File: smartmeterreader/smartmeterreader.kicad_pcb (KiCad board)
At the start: 2 copper layers, 54 x 44 mm, 50 parts, among them J1 USB_B_Micro_RA, J2 RJ12, Q1 2N7002NXBK, Q2 2N7002NXBK, Q3 PMV75UP, Q4 2N7002NXBK, Q5 PMV75UP, Q6 2N7002NXBK, SW1 SPST_NO, SW2 SPST_NO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

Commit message: Sync PCB with schematics
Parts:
- added D1: PMEG2010ER, Diode_SMD:D_SOD-123, F.Cu at (125.5, 90.2)
- added D7: Green, LED_SMD:LED_0603_1608Metric, F.Cu at (140.8, 93.2)
- added D8: Green, LED_SMD:LED_0603_1608Metric, F.Cu at (147.3, 103.8)
- added F1: 1A, Fuse:Fuse_1206_3216Metric, F.Cu at (130.2, 87.5)
- added F2: 1A, Fuse:Fuse_1206_3216Metric, F.Cu at (133.5, 109.2)
- added J3: 1x05_Pin_2.54mm, Connector_PinHeader_2.54mm:PinHeader_1x05_P2.54mm_Vertical, F.Cu at (146.8, 86.8)
- added R20: 1K, Resistor_SMD:R_0603_1608Metric, F.Cu at (140.7, 95.0)
- added R21: 1K, Resistor_SMD:R_0603_1608Metric, F.Cu at (147.3, 102.2)
- added REF**: MountingHole_2.5mm, MountingHole:MountingHole_2.5mm, F.Cu at (141.0, 77.2)
- added REF**: MountingHole_2.5mm, MountingHole:MountingHole_2.5mm, F.Cu at (166.0, 115.8)
- JP1, JP2: moved to B.Cu
- SW1, SW2: footprint Button_Switch_SMD:SW_Push_1P1T_NO_CK_KMR2 -> MECH_Switch_SMD:SW_Push_1P1T_NO_CK_KMR2
- moved R16 50.1 mm to (123.8, 75.8), turned to 0 degrees
- moved JP1 48.9 mm to (146.6, 112.5), turned to 90 degrees
- moved JP2 44.2 mm to (146.6, 110.0), turned to 90 degrees
- moved C9 43.1 mm to (123.8, 77.8), turned to 0 degrees
- moved R11 33.6 mm to (158.6, 78.0), turned to 0 degrees
- moved Q5 31.6 mm to (153.4, 80.7), turned to 0 degrees
- moved R18 30.4 mm to (150.8, 80.7)
- moved C1 30.3 mm to (153.7, 90.2)
- moved R10 29.2 mm to (132.2, 79.2), turned to 180 degrees
- moved Q2 28.2 mm to (142.7, 86.8), turned to 0 degrees
- moved R17 28.1 mm to (140.8, 101.4)
- moved C10 27.1 mm to (163.6, 78.0), turned to 0 degrees
- moved D6 26.9 mm to (129.0, 79.2)
- moved R14 26.8 mm to (133.2, 113.0)
- moved Q3 26.0 mm to (138.2, 105.3), turned to 180 degrees
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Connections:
- D3 pad 3: (no net) -> unconnected-(D3-Pad3)
- D3 pad 4: (no net) -> unconnected-(D3-Pad4)
- D4 pad 3: (no net) -> /DATA_LINE
- D4 pad 4: /DATA_LINE -> unconnected-(D4-Pad4)
- D4 pad 6: (no net) -> unconnected-(D4-Pad6)
- J1 pad 1: /5V_USB -> Net-(J1-Pad1)
- J1 pad 4: (no net) -> unconnected-(J1-Pad4)
- J2 pad 1: /5V_meter -> Net-(J2-Pad1)
- J2 pad 4: (no net) -> unconnected-(J2-Pad4)
- U1 pad 10: (no net) -> unconnected-(U1-Pad10)
- U1 pad 11: (no net) -> unconnected-(U1-Pad11)
- U1 pad 12: (no net) -> unconnected-(U1-Pad12)
- U1 pad 13: (no net) -> Net-(U1-Pad13)
- U1 pad 14: (no net) -> unconnected-(U1-Pad14)
- U1 pad 17: (no net) -> unconnected-(U1-Pad17)
- U1 pad 2: (no net) -> unconnected-(U1-Pad2)
- U1 pad 5: (no net) -> unconnected-(U1-Pad5)
- U1 pad 7: (no net) -> unconnected-(U1-Pad7)
- U1 pad 9: (no net) -> unconnected-(U1-Pad9)
- U2 pad 1: (no net) -> unconnected-(U2-Pad1)
- U2 pad 10: (no net) -> unconnected-(U2-Pad10)
- U2 pad 11: (no net) -> unconnected-(U2-Pad11)
- U2 pad 12: (no net) -> unconnected-(U2-Pad12)
- U2 pad 15: (no net) -> unconnected-(U2-Pad15)
- U2 pad 16: (no net) -> unconnected-(U2-Pad16)
- U2 pad 17: (no net) -> unconnected-(U2-Pad17)
- U2 pad 18: (no net) -> /USB-UART-transceiver/UART_CTS
- U2 pad 22: (no net) -> /USB-UART-transceiver/UART_DSR
- U2 pad 24: (no net) -> unconnected-(U2-Pad24)
- U4 pad 3: (no net) -> unconnected-(U4-Pad3)
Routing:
- net +3V3: track 0.00 -> 76.5 mm, vias 0 -> 8
- net /Data_line_TTL: track 0.00 -> 54.8 mm, vias 0 -> 1
- net GND: track 0.00 -> 53.9 mm, vias 0 -> 27
- net /GPIO0: track 0.00 -> 53.4 mm
- net /UART_RX: track 0.00 -> 53.0 mm, vias 0 -> 1
- net /5V_USB: track 0.00 -> 43.9 mm, vias 0 -> 2
- net /UART_RTS: track 0.00 -> 41.8 mm, vias 0 -> 1
- net /5V_meter: track 0.00 -> 41.0 mm
- net /nRST: track 0.00 -> 40.0 mm, vias 0 -> 2
- net /DHT22_DATA: track 0.00 -> 37.2 mm
- net /UART_TX: track 0.00 -> 27.8 mm, vias 0 -> 2
- net /DATA_LINE: track 0.00 -> 24.5 mm, vias 0 -> 1
- net /U0_TXD: track 0.00 -> 24.0 mm
- net /DHT22_EN: track 0.00 -> 21.7 mm, vias 0 -> 2
- net /GPIO4: track 0.00 -> 19.5 mm
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- added copper zone on F.Cu, net +3V3
- added copper zone on F.Cu, net /5V_USB
- added copper zone on F.Cu, net /USB-UART-transceiver/3.3V
- added copper zone on F.Cu, net Earth
- added copper zone on F.Cu, net GND
- added copper zone on In1.Cu, net GND
- added copper zone on In2.Cu, net GND
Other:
- outline, holes or cut-outs redrawn
- copper layers 2 -> 4
- net class Default removed
- board text added: "(3.3V)"
- board text added: "DTR"
- board text added: "Flash"
- board text added: "GND"
- board text added: "Humidity sensor"
- board text added: "In the case USB/UART is not populated. To program, set the jumpers ON JP1 and JP2 to "to Microcontroller""
- board text added: "P1 Smart Meter V1"
- board text added: "P1 bypass"
- board text added: "Program/Debug port"
- board text added: "RTS"
- board text added: "Reset"
- board text added: "Rx"
- board text added: "To UART Transceiver"
- board text added: "To microcontroller"
- board text added: "Tx"

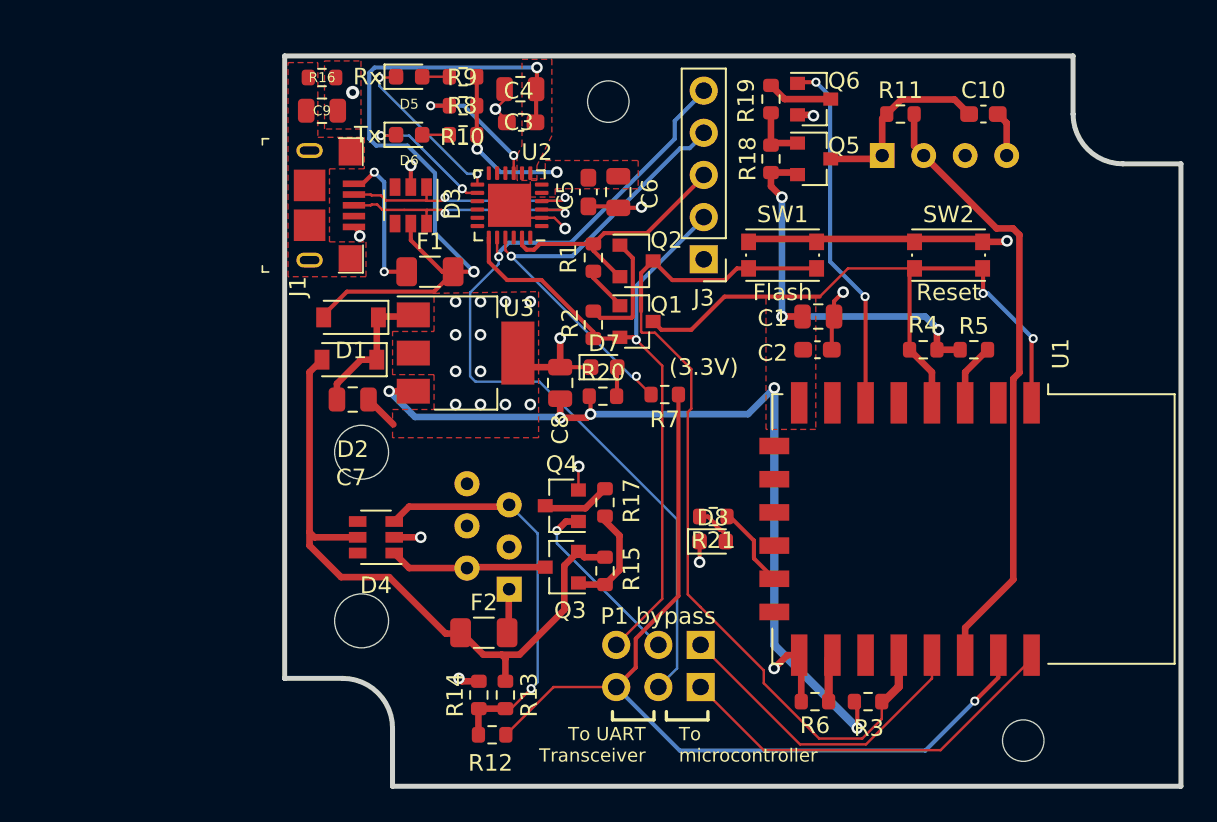
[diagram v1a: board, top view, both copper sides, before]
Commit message: Add readme, licensing and a little bit more information about the case
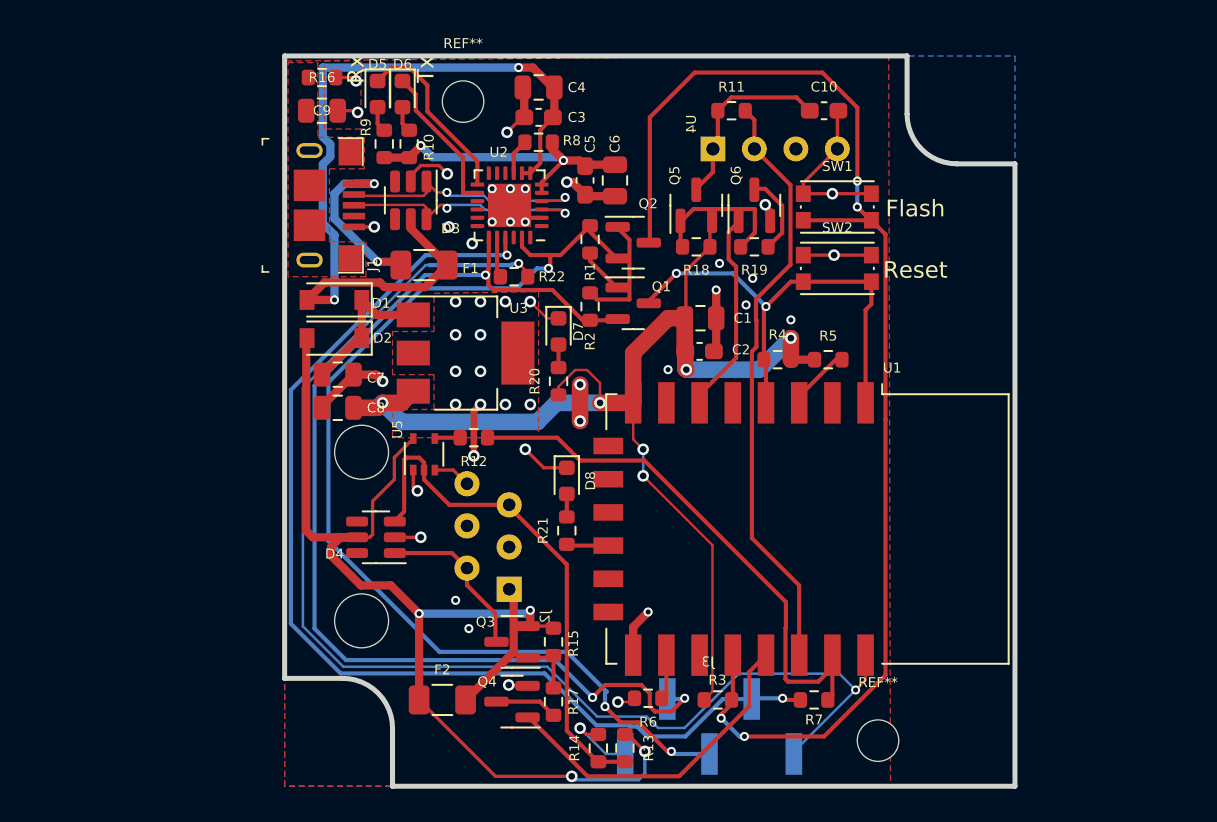
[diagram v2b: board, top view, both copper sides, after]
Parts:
- removed JP1, JP2: Jumper_3_ways, Connector_PinHeader_2.54mm:PinHeader_1x03_P2.54mm_Vertical
- removed the REF** at (141.0, 77.2)
- removed the REF** at (166.0, 115.8)
- added R22: 100R, Resistor_SMD:R_0603_1608Metric, F.Cu at (135.3, 87.8)
- added REF**: MountingHole_2.5mm, MountingHole:MountingHole_2.5mm, F.Cu at (157.2, 115.8)
- added REF**: MountingHole_2.5mm, MountingHole:MountingHole_2.5mm, F.Cu at (132.2, 77.2)
- added U5: 74HC1G02GW, Package_TO_SOT_SMD:SOT-353_SC-70-5, F.Cu at (129.9, 98.5)
- J3: value 1x05_Pin_2.54mm -> 1X05pin_2.54mm_smd; footprint Connector_PinHeader_2.54mm:PinHeader_1x05_P2.54mm_Vertical -> Connector_PinHeader_2.54mm:PinHeader_1x05_P2.54mm_Vertical_SMD_Pin1Right; moved to B.Cu
- R12: value 100R -> 10K
- R7: value 1K -> 100R
- moved J3 28.2 mm to (147.1, 114.9), turned to -90 degrees
- moved R7 20.5 mm to (153.4, 113.3), turned to 180 degrees
- moved R12 17.9 mm to (132.9, 97.5), turned to 180 degrees
- moved C8 13.5 mm to (124.7, 95.7), turned to 180 degrees
- moved R17 12.4 mm to (137.7, 113.4), turned to -90 degrees
- moved Q4 12.2 mm to (135.2, 113.4)
- moved U4 10.2 mm to (147.3, 80.1)
- moved R11 10.2 mm to (148.4, 77.8)
- moved R6 10.1 mm to (143.4, 113.2)
- moved U1 10.0 mm to (153.0, 103.0)
- moved C10 9.60 mm to (154.0, 77.8)
- moved D8 9.52 mm to (138.5, 100.1), turned to -90 degrees
- moved R3 9.05 mm to (147.6, 113.3)
- moved R19 8.96 mm to (149.8, 86.0), turned to 0 degrees
- moved R21 8.87 mm to (138.5, 103.1), turned to 90 degrees
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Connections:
- R12 pad 1: /DATA_LINE -> /Data_line_TTL
- R12 pad 2: /Data_line_TTL -> Net-(R12-Pad2)
- R21 pad 1: Net-(U1-Pad13) -> Net-(R21-Pad1)
- R7 pad 1: /UART_TX -> /Data_line_TTL
- R7 pad 2: /Data_line_TTL -> /UART_TX
- U1 pad 12: unconnected-(U1-Pad12) -> Net-(R21-Pad1)
- U1 pad 13: Net-(U1-Pad13) -> unconnected-(U1-Pad13)
- U1 pad 19: /GPIO4 -> /Data_Req_TTL
- U1 pad 22: /U0_TXD -> /UART_RX
- U2 pad 20: /UART_RX -> /USB-UART-transceiver/UART_RX
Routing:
- net /UART_DTR: track 16.0 -> 63.7 mm, vias 0 -> 3
- net /UART_TX: track 27.8 -> 66.1 mm
- net /UART_RTS: track 41.8 -> 66.2 mm, vias 1 -> 3
- net /5V_meter: track 41.0 -> 65.5 mm, vias 0 -> 4
- net /U0_TXD: track 24.0 -> 0.00 mm
- net /UART_RX: track 53.0 -> 76.8 mm, vias 1 -> 2
- net /GPIO0: track 53.4 -> 77.0 mm, vias 0 -> 4
- net /Data_line_TTL: track 54.8 -> 33.5 mm, vias 1 -> 0
- net /GPIO4: track 19.5 -> 0.00 mm
- net /nRST: track 40.0 -> 29.2 mm
- net GND: track 53.9 -> 63.7 mm, vias 27 -> 48
- net /DHT22_EN: track 21.7 -> 12.2 mm, vias 2 -> 0
- net /Data_Req_TTL: track 10.9 -> 20.0 mm, vias 1 -> 0
- net /USB-UART-transceiver/3.3V: track 9.74 -> 18.6 mm
- net /DATA_LINE: track 24.5 -> 31.5 mm, vias 1 -> 0
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- added copper zone on B.Cu, net GND
- removed copper zone on F.Cu, net +3V3
- removed copper zone on F.Cu, net /5V_USB
- removed copper zone on F.Cu, net /USB-UART-transceiver/3.3V
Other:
- board size 54 x 44 mm -> 44 x 44 mm
- board text removed: "(3.3V)"
- board text removed: "P1 bypass"
- board text removed: "To UART Transceiver"
- board text removed: "To microcontroller"
